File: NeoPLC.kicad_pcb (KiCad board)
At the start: 2 copper layers, 75 x 110 mm, 39 parts, among them J1 Backplane 2x6, J2 DI1-4+COM 3.5mm, J3 DI5-8+COM 3.5mm, J4 SWD, U1 STM32G071CBT6, U2 AP2112K-3.3, U3 ISL3178EIBZ, U4 TLP291-4, U5 TLP291-4, Y1 8MHz

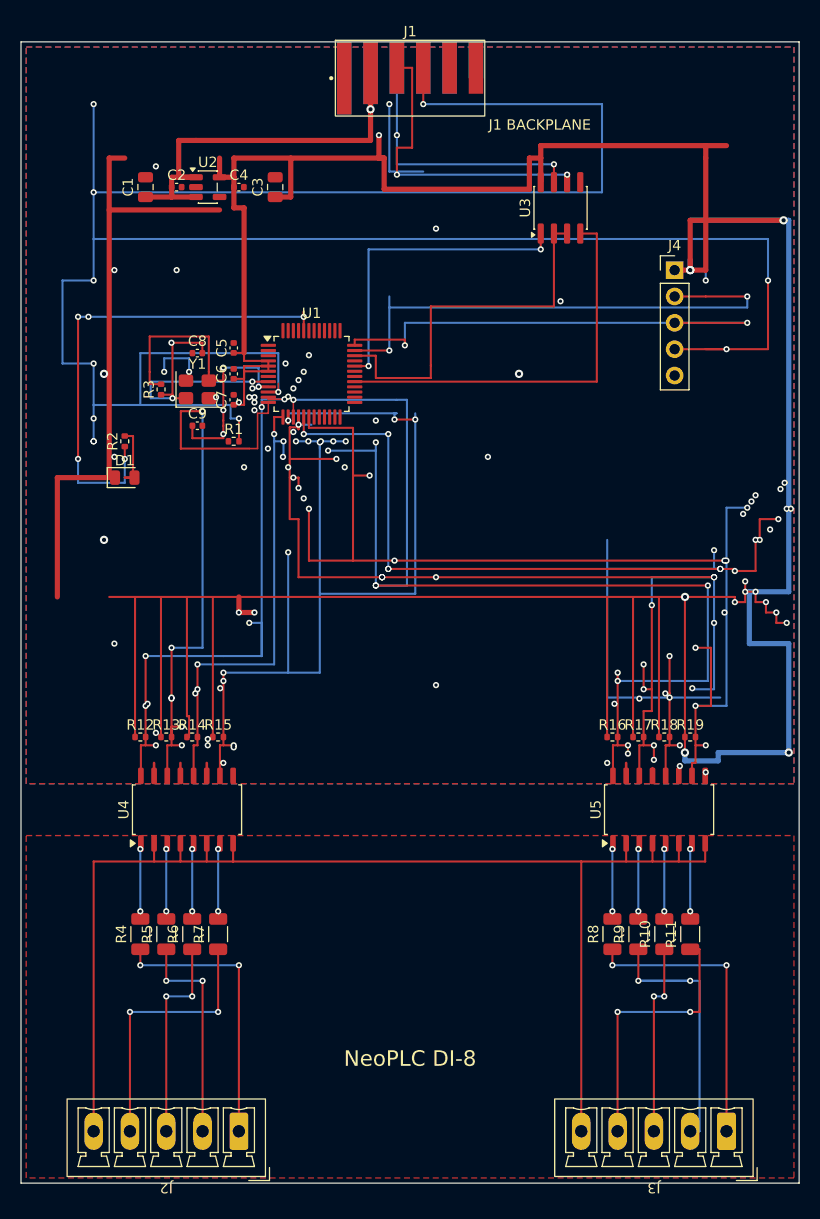
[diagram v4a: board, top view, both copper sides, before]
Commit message: Saha FIELD_COM arka pour ve DI2 ada dikişi: DRC yine 74.
Izole ada F/B birleşti; DI8_IN via’dan kaçırıldı. Silinemeyen via kısa devreleri aynı üç çift.

Co-authored-by: Cursor <cursoragent@cursor.com>
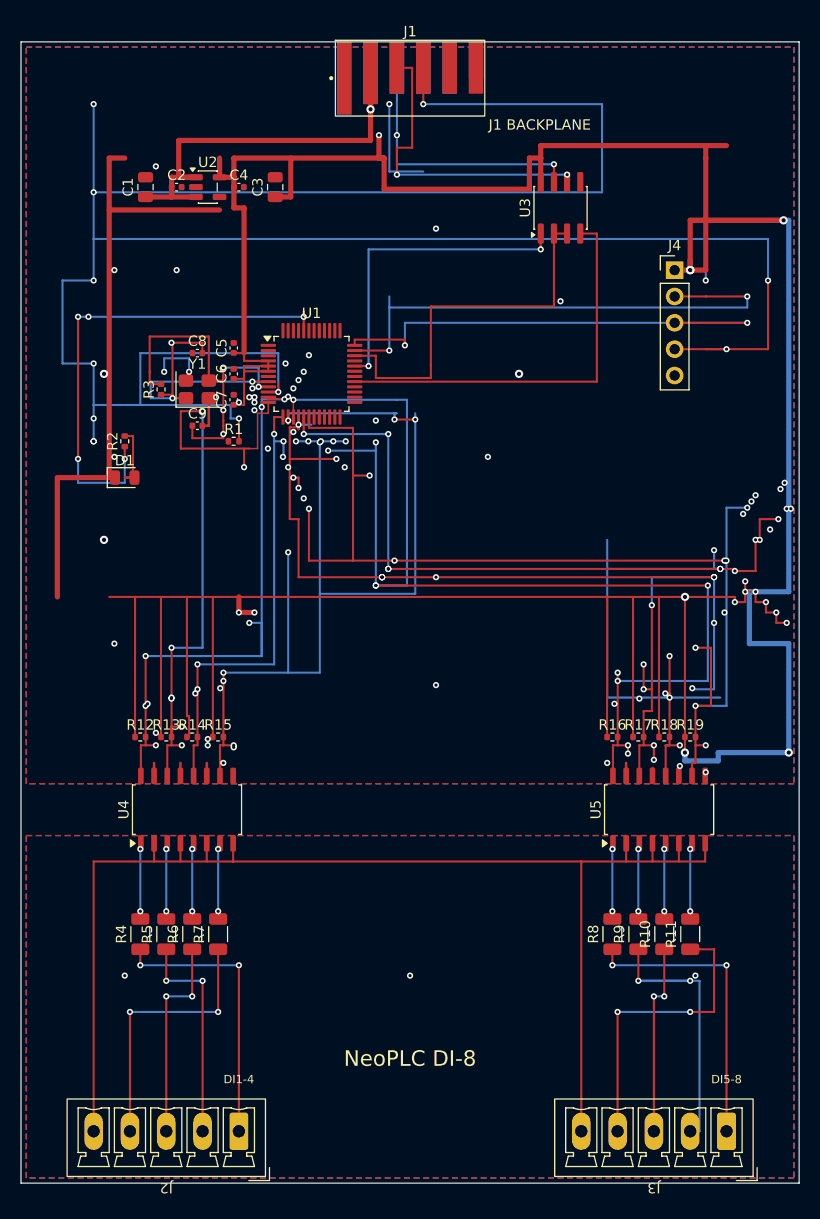
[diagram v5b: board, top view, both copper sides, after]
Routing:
- net GND: track 71.5 -> 74.8 mm
- net /DI Field/DI8_IN: track 26.3 -> 29.1 mm
- net /DI Field/DI2: track 60.1 -> 61.9 mm
- net /DI Field/FIELD_COM: vias 0 -> 3
- added copper zone on B.Cu, net /DI Field/FIELD_COM
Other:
- board text added: "DI1-4"
- board text added: "DI5-8"
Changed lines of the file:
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@@
 		(layer "Edge.Cuts")
 	)
+	(gr_text "DI1-4"
+		(at 21 100 0)
+		(layer "F.SilkS")
+		(effects
+			(font
+				(size 0.8 0.8)
+				(thickness 0.12)
+			)
+		)
+	)
+	(gr_text "DI5-8"
+		(at 68 100 0)
+		(layer "F.SilkS")
+		(effects
+			(font
+				(size 0.8 0.8)
+				(thickness 0.12)
+			)
+		)
+	)
 	(gr_text "J1 BACKPLANE"
 		(at 50 8 0)
@@
 	)
 	(segment
+		(start 21.5 41)
+		(end 21.5 39.2)
+		(width 0.2)
+		(layer "F.Cu")
+		(net "/DI Field/DI2")
+	)
+	(segment
 		(start 15.4 35.6)
 		(end 15.4 39.2)
@@
 	)
 	(segment
+		(start 18.1 37)
+		(end 18.1 34.35)
+		(width 0.25)
+		(layer "F.Cu")
+		(net "GND")
+	)
+	(segment
 		(start 12.825 70.75)
 		(end 12.825 69.5)
@@
 	)
 	(segment
+		(start 17.48 37)
+		(end 18.1 37)
+		(width 0.25)
+		(layer "F.Cu")
+		(net "GND")
+	)
+	(segment
 		(start 60.865 70.75)
 		(end 60.865 70)
@@
 		(net "/DI Field/FIELD_COM")
 	)
+	(via
+		(at 10 90)
+		(size 0.6)
+		(drill 0.3)
+		(layers "F.Cu" "B.Cu")
+		(net "/DI Field/FIELD_COM")
+	)
+	(via
+		(at 65 90)
+		(size 0.6)
+		(drill 0.3)
+		(layers "F.Cu" "B.Cu")
+		(net "/DI Field/FIELD_COM")
+	)
+	(via
+		(at 37.5 90)
+		(size 0.6)
+		(drill 0.3)
+		(layers "F.Cu" "B.Cu")
+		(net "/DI Field/FIELD_COM")
+	)
 	(segment
 		(start 62 84.5375)
@@
 	(segment
 		(start 65.4 93.5)
+		(end 66.8 93.5)
+		(width 0.2)
+		(layer "F.Cu")
+		(net "/DI Field/DI8_IN")
+	)
+	(segment
+		(start 66.8 87.4625)
 		(end 65.4 87.4625)
 		(width 0.2)
@@
 	)
 	(segment
+		(start 66.8 93.5)
+		(end 66.8 87.4625)
+		(width 0.2)
+		(layer "F.Cu")
+		(net "/DI Field/DI8_IN")
+	)
+	(segment
 		(start 64.5 93.5)
 		(end 65.4 93.5)
@@
 			)
 		)
+	)
+	(zone
+		(net "/DI Field/FIELD_COM")
+		(layer "B.Cu")
+		(name "FIELD_COM_B")
+		(hatch edge 0.508)
+		(connect_pads
+			(clearance 0.3)
+		)
+		(min_thickness 0.2)
+		(fill yes
+			(thermal_gap 0.5)
+			(thermal_bridge_width 0.5)
+			(island_removal_mode 0)
+		)
+		(polygon
+			(pts
+				(xy 0.5 76.5) (xy 74.5 76.5) (xy 74.5 109.5) (xy 0.5 109.5)
+			)
+		)

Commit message: DI2/+3V3 ada dikişi, COM ipek ve GND via’lar: DRC 74→73.
Doğu +3V3 omurgaya bağlandı; DI7 doğu via’sı last-mile’a girdi. Silinemeyen üç via kısa devresi aynı.

Co-authored-by: Cursor <cursoragent@cursor.com>
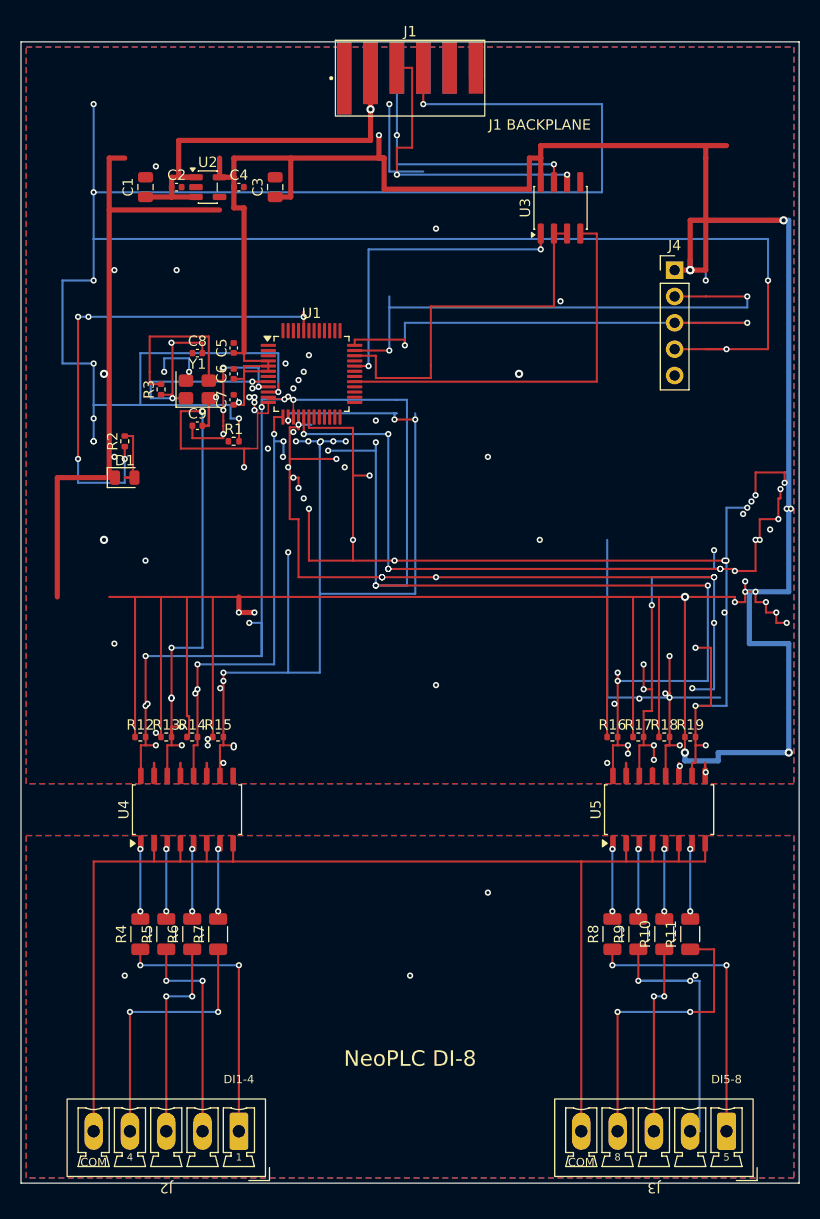
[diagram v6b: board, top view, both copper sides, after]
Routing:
- net +3V3: track 397.6 -> 404.0 mm
- net GND: track 74.8 -> 77.9 mm, vias 21 -> 23
- net /DI Field/DI7: track 118.7 -> 121.8 mm
- net /DI Field/DI2: track 61.9 -> 63.3 mm
- net /DI Field/FIELD_COM: vias 3 -> 4
- net /DI Field/DI8: vias 10 -> 11
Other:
- board text added: "1"
- board text added: "4"
- board text added: "5"
- board text added: "8"
- board text added: "COM"
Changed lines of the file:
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@@
 		(layer "Edge.Cuts")
+	)
+	(gr_text "4"
+		(at 10.5 107.5 0)
+		(layer "F.SilkS")
+		(effects
+			(font
+				(size 0.7 0.7)
+				(thickness 0.105)
+			)
+		)
+	)
+	(gr_text "1"
+		(at 21 107.5 0)
+		(layer "F.SilkS")
+		(effects
+			(font
+				(size 0.7 0.7)
+				(thickness 0.105)
+			)
+		)
+	)
+	(gr_text "8"
+		(at 57.5 107.5 0)
+		(layer "F.SilkS")
+		(effects
+			(font
+				(size 0.7 0.7)
+				(thickness 0.105)
+			)
+		)
+	)
+	(gr_text "5"
+		(at 68 107.5 0)
+		(layer "F.SilkS")
+		(effects
+			(font
+				(size 0.7 0.7)
+				(thickness 0.105)
+			)
+		)
+	)
+	(gr_text "COM"
+		(at 7 108 0)
+		(layer "F.SilkS")
+		(effects
+			(font
+				(size 0.8 0.8)
+				(thickness 0.12)
+			)
+		)
 	)
 	(gr_text "DI1-4"
@@
 		)
 	)
+	(gr_text "COM"
+		(at 54 108 0)
+		(layer "F.SilkS")
+		(effects
+			(font
+				(size 0.8 0.8)
+				(thickness 0.12)
+			)
+		)
+	)
 	(gr_text "DI5-8"
 		(at 68 100 0)
@@
 	)
 	(segment
+		(start 73.6 41.5)
+		(end 73.6 42.5)
+		(width 0.2)
+		(layer "F.Cu")
+		(net "+3V3")
+	)
+	(segment
 		(start 66 10)
 		(end 66 11.2)
@@
 	)
 	(segment
+		(start 70.8 41.5)
+		(end 73.6 41.5)
+		(width 0.2)
+		(layer "F.Cu")
+		(net "+3V3")
+	)
+	(segment
 		(start 72.8 55)
 		(end 72.8 56)
@@
 		(end 21.5 16)
 		(width 0.5)
+		(layer "F.Cu")
+		(net "+3V3")
+	)
+	(segment
+		(start 70.8 43.7)
+		(end 70.8 41.5)
+		(width 0.2)
 		(layer "F.Cu")
 		(net "+3V3")
@@
 	)
 	(segment
+		(start 73.6 41.5)
+		(end 74 41.5)
+		(width 0.2)
+		(layer "B.Cu")
+		(net "+3V3")
+	)
+	(segment
 		(start 67.2 68.5)
 		(end 67.2 69.3)
@@
 	)
 	(segment
+		(start 22.5 34.75)
+		(end 22.5 35.5)
+		(width 0.15)
+		(layer "F.Cu")
+		(net "/DI Field/DI2")
+	)
+	(segment
 		(start 14.51 67)
 		(end 14.51 66)
 		(width 0.2)
+		(layer "F.Cu")
+		(net "/DI Field/DI2")
+	)
+	(segment
+		(start 22.5 35.5)
+		(end 22.8 35.5)
+		(width 0.15)
 		(layer "F.Cu")
 		(net "/DI Field/DI2")
@@
 	)
 	(segment
+		(start 22.8 35.5)
+		(end 22.8 35.8)
+		(width 0.15)
+		(layer "F.Cu")
+		(net "/DI Field/DI2")
+	)
+	(segment
 		(start 14.51 67.8)
 		(end 15.5 67.8)
@@
 	)
 	(segment
+		(start 65.944999 70.75)
+		(end 65.944999 69.5)
+		(width 0.25)
+		(layer "F.Cu")
+		(net "GND")
+	)
+	(segment
+		(start 23.8375 32.25)
+		(end 23.2 32.25)
+		(width 0.2)
+		(layer "F.Cu")
+		(net "GND")
+	)
+	(segment
 		(start 18.8 34.35)
 		(end 18.8 34.25)
@@
 	)
 	(segment
+		(start 63.405 70.75)
+		(end 63.405 69.5)
+		(width 0.25)
+		(layer "F.Cu")
+		(net "GND")
+	)
+	(segment
 		(start 17.48 37)
 		(end 18.1 37)
@@
 	)
 	(via
+		(at 50 48)
+		(size 0.6)
+		(drill 0.3)
+		(layers "F.Cu" "B.Cu")
+		(net "GND")
+	)
+	(via
 		(at 13 12)
 		(size 0.6)
@@
 	)
 	(via
+		(at 12 50)
+		(size 0.6)
+		(drill 0.3)
+		(layers "F.Cu" "B.Cu")
+		(net "GND")
+	)
+	(via
 		(at 16.2 31.8)
 		(size 0.6)
@@
 	)
 	(via
+		(at 45 82)
+		(size 0.6)
+		(drill 0.3)
+		(layers "F.Cu" "B.Cu")
+		(net "/DI Field/FIELD_COM")
+	)
+	(via
 		(at 37.5 90)
 		(size 0.6)
@@
 	)
 	(via
+		(at 32 48)
+		(size 0.6)
+		(drill 0.3)
+		(layers "F.Cu" "B.Cu")
+		(net "/DI Field/DI8")
+	)
+	(via
 		(at 70 44.9)
 		(size 0.6)
@@
 	)
 	(segment
+		(start 73.2 44)
+		(end 73.2 43.1)
+		(width 0.2)
+		(layer "F.Cu")
+		(net "/DI Field/DI7")
+	)
+	(segment
 		(start 62.51 67)
 		(end 62.51 63.2)
@@
 	)
 	(segment
+		(start 73 44)
+		(end 73.2 44)
+		(width 0.2)
+		(layer "F.Cu")
+		(net "/DI Field/DI7")
+	)
+	(segment
 		(start 68.8 50.8)
 		(end 68.8 51)
@@
 		(width 0.2)
 		(layer "F.Cu")
+		(net "/DI Field/DI7")
+	)
+	(segment
+		(start 73 46)
+		(end 73 44)
+		(width 0.2)
+		(layer "F.Cu")

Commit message: DI5 ada via 34.2 dikişi ve C5 GND pour: DRC 73→77.
Doğu DI6 hop +3V3/DI8’e girdi, geri alındı. 15.9,30 via RST# oldu (silinemez). Üç kısa devre aynı.

Co-authored-by: Cursor <cursoragent@cursor.com>
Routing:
- net +3V3: track 404.0 -> 426.9 mm, vias 23 -> 24
- net /DI Field/DI5: track 114.0 -> 120.0 mm
- net GND: track 77.9 -> 81.4 mm, vias 23 -> 22
- net +5V: track 42.8 -> 45.3 mm, vias 1 -> 2
- net /Node Core/MOD_RST#: vias 13 -> 14
- net /DI Field/DI6: vias 21 -> 20
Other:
- board text added: "ISO"
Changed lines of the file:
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@@
 		)
 	)
+	(gr_text "ISO"
+		(at 37.5 74 0)
+		(layer "F.SilkS")
+		(effects
+			(font
+				(size 0.8 0.8)
+				(thickness 0.12)
+			)
+		)
+	)
 	(gr_text "COM"
 		(at 54 108 0)
@@
 	)
 	(via
+		(at 72.2 47)
+		(size 0.6)
+		(drill 0.3)
+		(layers "F.Cu" "B.Cu")
+		(net "+3V3")
+	)
+	(via
 		(at 18 67.2)
 		(size 0.6)
@@
 	)
 	(segment
+		(start 72.2 47)
+		(end 72.2 53.5)
+		(width 0.2)
+		(layer "B.Cu")
+		(net "+3V3")
+	)
+	(segment
 		(start 70.2 58)
 		(end 74 58)
@@
 	)
 	(segment
+		(start 72.2 47)
+		(end 72.2 42)
+		(width 0.2)
+		(layer "B.Cu")
+		(net "+3V3")
+	)
+	(segment
 		(start 67.2 69.3)
 		(end 63.99 69.3)
@@
 	)
 	(segment
+		(start 72.2 42)
+		(end 60.8 42)
+		(width 0.2)
+		(layer "B.Cu")
+		(net "+3V3")
+	)
+	(segment
 		(start 22.5 34.75)
 		(end 22.5 35.5)
@@
 	)
 	(segment
+		(start 15.48 12)
+		(end 13 12)
+		(width 0.25)
+		(layer "F.Cu")
+		(net "+5V")
+	)
+	(segment
 		(start 14.52 14)
 		(end 14.52 14.95)
@@
 	)
 	(via
+		(at 13 12)
+		(size 0.6)
+		(drill 0.3)
+		(layers "F.Cu" "B.Cu")
+		(net "+5V")
+	)
+	(via
 		(at 33.69 6.5)
 		(size 0.8)
@@
 	)
 	(segment
+		(start 20.445 70.75)
+		(end 20.445 70)
+		(width 0.25)
+		(layer "F.Cu")
+		(net "GND")
+	)
+	(segment
 		(start 8 32)
 		(end 8.5 32)
@@
 	)
 	(segment
+		(start 20.5 29.02)
+		(end 19.3 29.02)
+		(width 0.25)
+		(layer "F.Cu")
+		(net "GND")
+	)
+	(segment
 		(start 17.48 37)
 		(end 18.1 37)
@@
 	)
 	(segment
+		(start 19.3 29.02)
+		(end 19.3 27.5)
+		(width 0.25)
+		(layer "F.Cu")
+		(net "GND")
+	)
+	(segment
 		(start 60.865 70.75)
 		(end 60.865 70)
@@
 	)
 	(via
-		(at 13 12)
-		(size 0.6)
-		(drill 0.3)
-		(layers "F.Cu" "B.Cu")
-		(net "GND")
-	)
-	(via
 		(at 45 40)
 		(size 0.6)
@@
 	)
 	(via
-		(at 72.2 47)
-		(size 0.6)
-		(drill 0.3)
-		(layers "F.Cu" "B.Cu")
-		(net "/DI Field/DI6")
-	)
-	(via
 		(at 30.4 40.2)
 		(size 0.6)
@@
 	)
 	(segment
+		(start 34.2 36.5)
+		(end 34.2 37)
+		(width 0.2)
+		(layer "B.Cu")
+		(net "/DI Field/DI5")
+	)
+	(segment
 		(start 34.2 52.4)
 		(end 34.2 38.6)
@@
 	)
 	(segment
+		(start 34.2 37)
+		(end 37.2 37)
+		(width 0.2)
+		(layer "B.Cu")
+		(net "/DI Field/DI5")
+	)
+	(segment
 		(start 31.4 34.5)
 		(end 36.2 34.5)
@@
 	)
 	(segment
+		(start 37.2 37)
+		(end 37.2 34.5)
+		(width 0.2)
+		(layer "B.Cu")
+		(net "/DI Field/DI5")
+	)
+	(segment
 		(start 37.2 34.5)
 		(end 37.2 52.4)
@@
 		(size 0.6)
 		(drill 0.3)
+		(layers "F.Cu" "B.Cu")
+		(net "/Node Core/MOD_RST#")
+	)
+	(via
+		(at 15.9 30)
+		(size 0.6)
+		(drill 0.3)

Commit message: Konnect delete_via eksiği için IPC köprü; pad-yanı via’lar silindi, DRC 69→54.
Co-authored-by: Cursor <cursoragent@cursor.com>
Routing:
- net /DI Field/DI1: track 57.3 -> 55.5 mm, vias 8 -> 5
- net /DI Field/DI3: track 45.7 -> 47.0 mm
- net /DI Field/DI6: track 110.1 -> 109.4 mm, vias 20 -> 18
- net /DI Field/DI4: track 100.8 -> 100.4 mm, vias 17 -> 16
- net /Node Core/MOD_RST#: vias 14 -> 13
- net /DI Field/DI7: vias 20 -> 19
- net /DI Field/DI5: vias 13 -> 12
- net /DI Field/DI2: vias 11 -> 8
- net +3V3: vias 24 -> 23
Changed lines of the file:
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@@
 	)
 	(via
-		(at 18 67.2)
-		(size 0.6)
-		(drill 0.3)
-		(layers "F.Cu" "B.Cu")
-		(net "+3V3")
-	)
-	(via
 		(at 72.8 55)
 		(size 0.6)
@@
 	)
 	(via
-		(at 22 34.25)
-		(size 0.6)
-		(drill 0.3)
-		(layers "F.Cu" "B.Cu")
-		(net "/DI Field/DI2")
-	)
-	(via
-		(at 22.5 34.75)
-		(size 0.6)
-		(drill 0.3)
-		(layers "F.Cu" "B.Cu")
-		(net "/DI Field/DI2")
-	)
-	(via
 		(at 14.5 63.3)
 		(size 0.6)
@@
 	)
 	(via
-		(at 22.5 34.25)
-		(size 0.6)
-		(drill 0.3)
-		(layers "F.Cu" "B.Cu")
-		(net "/DI Field/DI2")
-	)
-	(via
 		(at 15.5 66)
 		(size 0.6)
@@
 	)
 	(segment
+		(start 16.635 67.8)
+		(end 18 67.8)
+		(width 0.2)
+		(layer "F.Cu")
+		(net "/DI Field/DI3")
+	)
+	(segment
 		(start 17.01 67.8)
 		(end 17.01 67)
@@
 	)
 	(via
-		(at 27.25 31.8)
-		(size 0.6)
-		(drill 0.3)
-		(layers "F.Cu" "B.Cu")
-		(net "/DI Field/DI7")
-	)
-	(via
 		(at 27.25 44)
 		(size 0.6)
@@
 	)
 	(segment
-		(start 26.75 36.9)
-		(end 26.75 36.1625)
-		(width 0.2)
-		(layer "F.Cu")
-		(net "/DI Field/DI6")
-	)
-	(segment
 		(start 34.8 51.6)
 		(end 26.75 51.6)
@@
 	)
 	(via
-		(at 26.75 32.6)
-		(size 0.6)
-		(drill 0.3)
-		(layers "F.Cu" "B.Cu")
-		(net "/DI Field/DI6")
-	)
-	(via
 		(at 25.75 41)
 		(size 0.6)
@@
 	)
 	(via
-		(at 26.75 36.9)
-		(size 0.6)
-		(drill 0.3)
-		(layers "F.Cu" "B.Cu")
-		(net "/DI Field/DI6")
-	)
-	(via
 		(at 60.01 60)
 		(size 0.6)
@@
 	)
 	(via
-		(at 26.25 34.5)
-		(size 0.6)
-		(drill 0.3)
-		(layers "F.Cu" "B.Cu")
-		(net "/DI Field/DI5")
-	)
-	(via
 		(at 34.2 38.6)
 		(size 0.6)
@@
 	)
 	(via
-		(at 15.9 30)
-		(size 0.6)
-		(drill 0.3)
-		(layers "F.Cu" "B.Cu")
-		(net "/Node Core/MOD_RST#")
-	)
-	(via
 		(at 7 36.3)
 		(size 0.6)
@@
 	)
 	(segment
-		(start 23.8375 34.45)
-		(end 23.8375 34.25)
-		(width 0.15)
-		(layer "F.Cu")
-		(net "/DI Field/DI1")
-	)
-	(segment
-		(start 25.4 34.45)
-		(end 23.8375 34.45)
-		(width 0.15)
-		(layer "F.Cu")
-		(net "/DI Field/DI1")
-	)
-	(segment
 		(start 11.555 67.8)
 		(end 12.01 67.8)
@@
 	)
 	(via
-		(at 23.2 35.2)
-		(size 0.6)
-		(drill 0.3)
-		(layers "F.Cu" "B.Cu")
-		(net "/DI Field/DI1")
-	)
-	(via
 		(at 13 67.8)
 		(size 0.6)
@@
 	)
 	(via
-		(at 25.75 34.2)
-		(size 0.6)
-		(drill 0.3)
-		(layers "F.Cu" "B.Cu")
-		(net "/DI Field/DI1")
-	)
-	(via
 		(at 12.2 63.8)
 		(size 0.6)
@@
 	)
 	(via
-		(at 25.4 34.45)
-		(size 0.6)
-		(drill 0.3)
-		(layers "F.Cu" "B.Cu")
-		(net "/DI Field/DI1")
-	)
-	(via
 		(at 12.01 59.2)
 		(size 0.6)
@@
 	)
 	(segment
-		(start 25.75 36.5)
-		(end 25.75 36.1625)
-		(width 0.2)
-		(layer "F.Cu")
-		(net "/DI Field/DI4")
-	)
-	(segment
 		(start 19.51 67)
 		(end 19.51 60.8)
@@
 		(size 0.6)
 		(drill 0.3)
-		(layers "F.Cu" "B.Cu")
-		(net "/DI Field/DI4")
-	)
-	(via
-		(at 25.75 36.5)
-		(size 0.6)
-		(drill 0.3)
